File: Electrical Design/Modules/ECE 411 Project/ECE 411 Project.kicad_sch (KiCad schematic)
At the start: 11 parts, among them J1 NJ2FD-V, J2 Conn_01x02_Pin, Q7 PNP, U1 ESP32-C3-WROOM-02, U10 MN3207, U2 LM555xM, U4 PAM8406D, U6 TL072

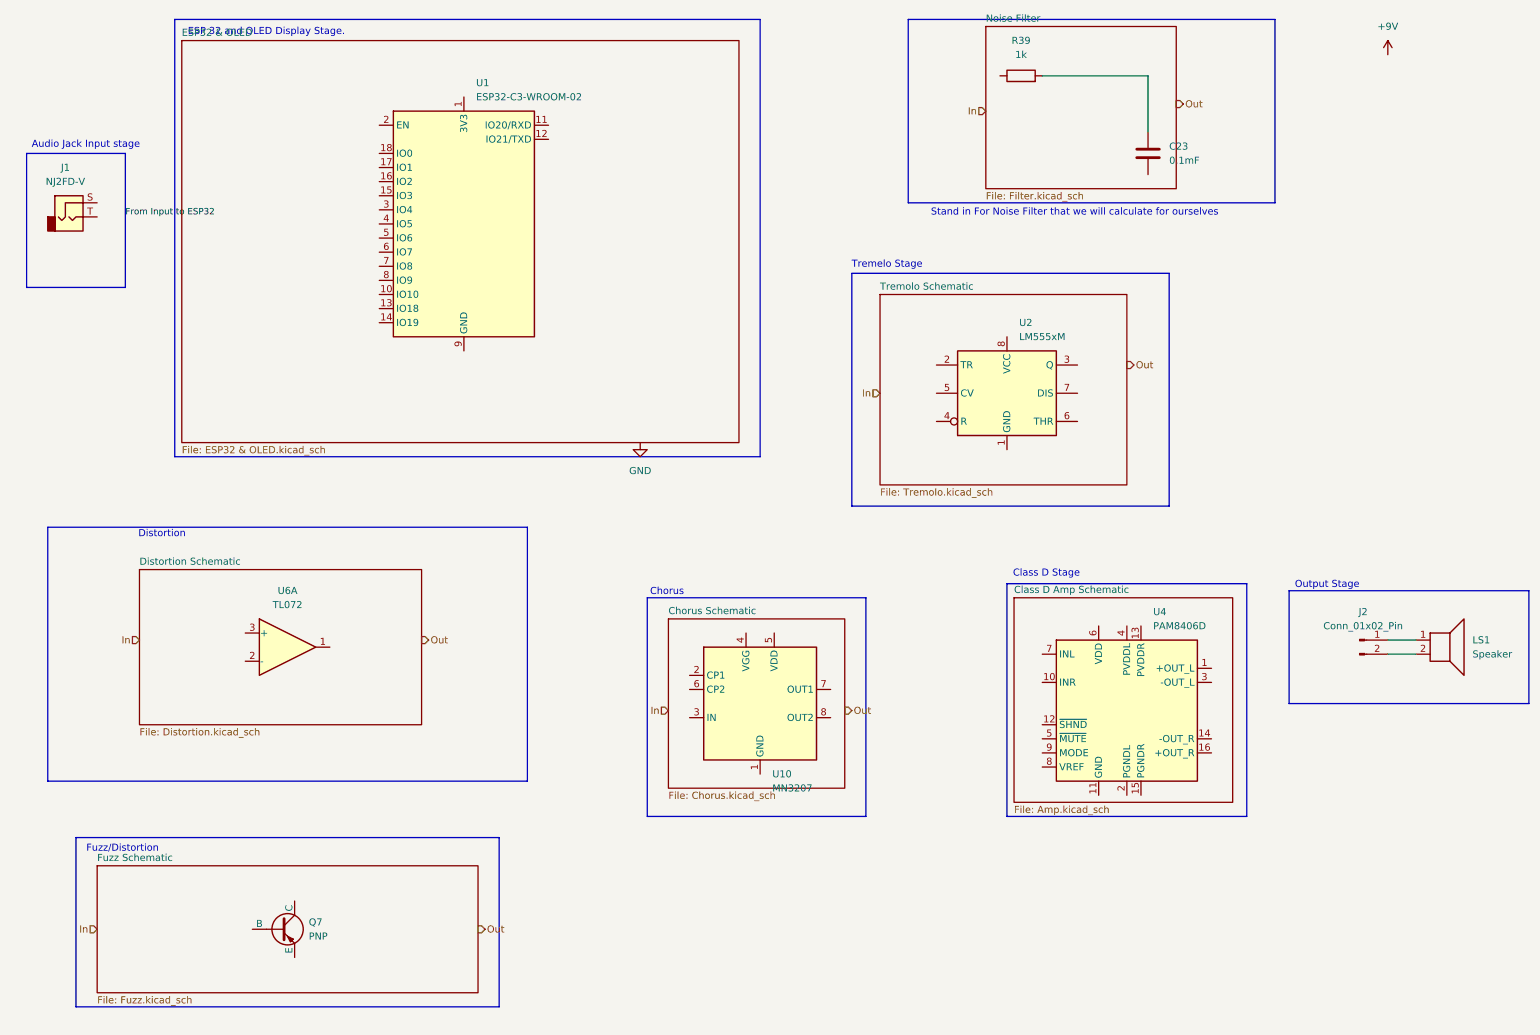
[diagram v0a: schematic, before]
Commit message: Minor changes to schematic wiring
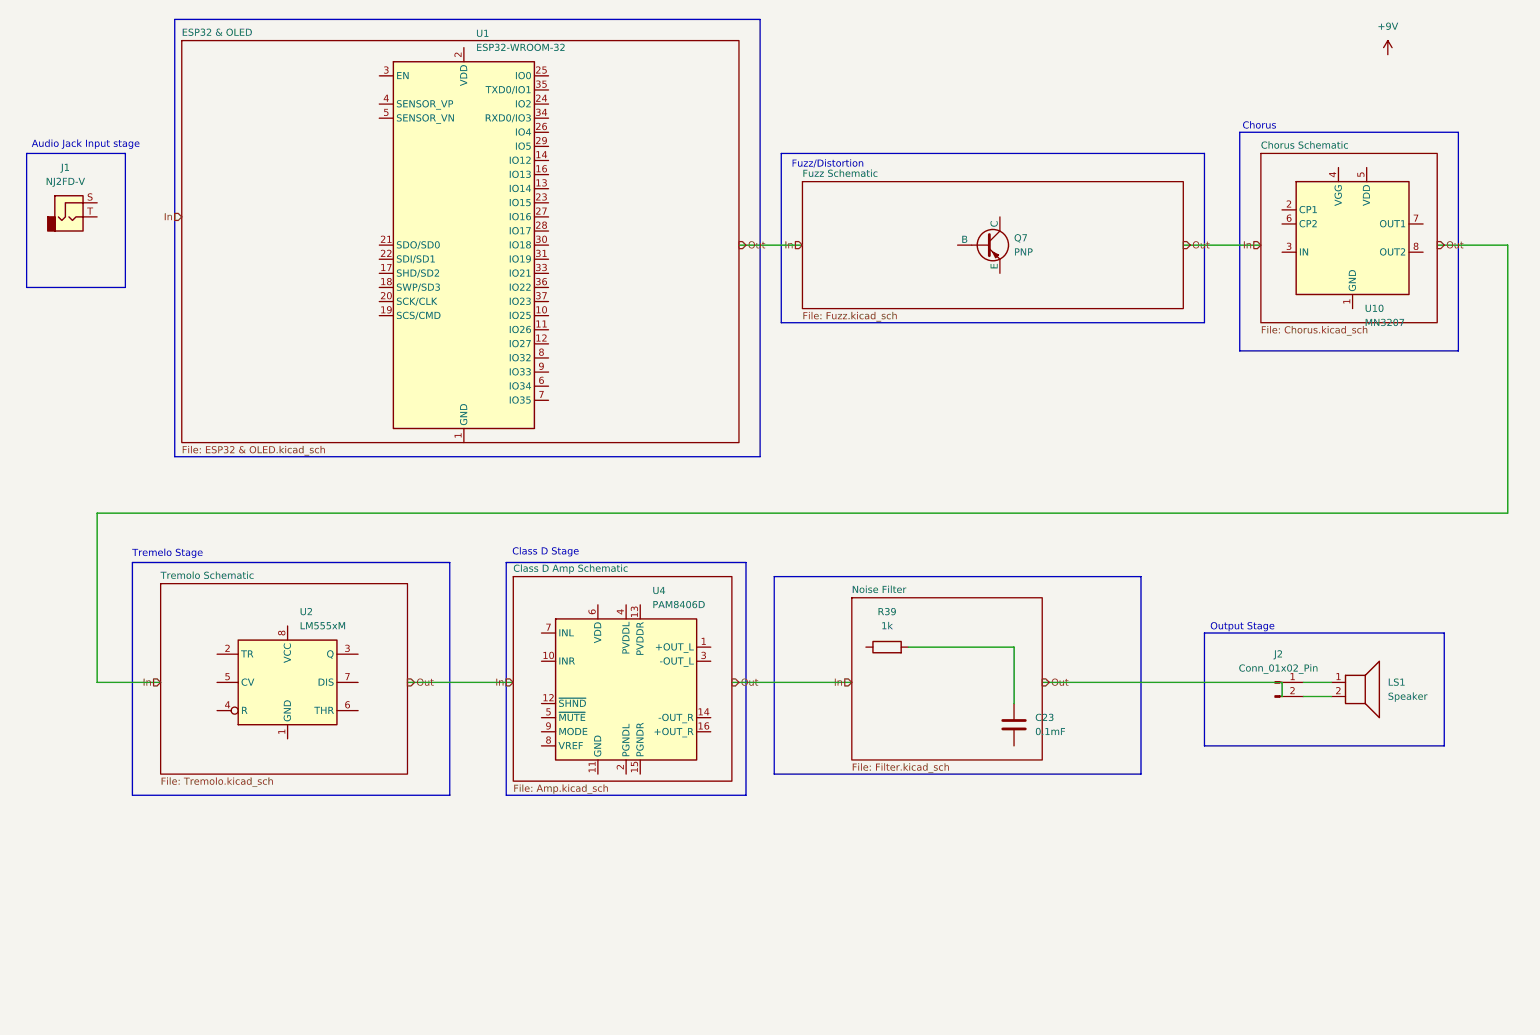
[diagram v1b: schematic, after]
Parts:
- removed U1: ESP32-C3-WROOM-02, RF_Module:ESP32-C3-WROOM-02, symbol RF_Module:ESP32-C3-WROOM-02
- removed U6: TL072, symbol Amplifier_Operational:TL072
- added U1: ESP32-WROOM-32, RF_Module:ESP32-WROOM-32, symbol RF_Module:ESP32-WROOM-32
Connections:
- new net: U1.1 (GND), U1.15 (GND), U1.38 (GND), U1.39 (GND)
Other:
- removed sheet Distortion Schematic
- note removed: "Distortion"
- note removed: "ESP 32 and OLED Display Stage."
- note removed: "Stand in For Noise Filter that we will calculate for ourselves"
- moved on the sheet: C23, J2, LS1, Q7, R39, U10, U2, U4

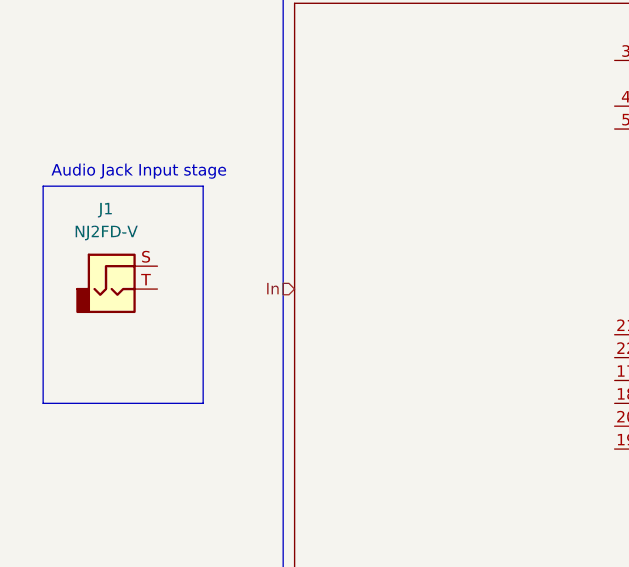
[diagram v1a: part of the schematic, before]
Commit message: Final Touches to Preliminary Schematic
Created Symbol for Small OLED screen and finalized input/output connections for each module
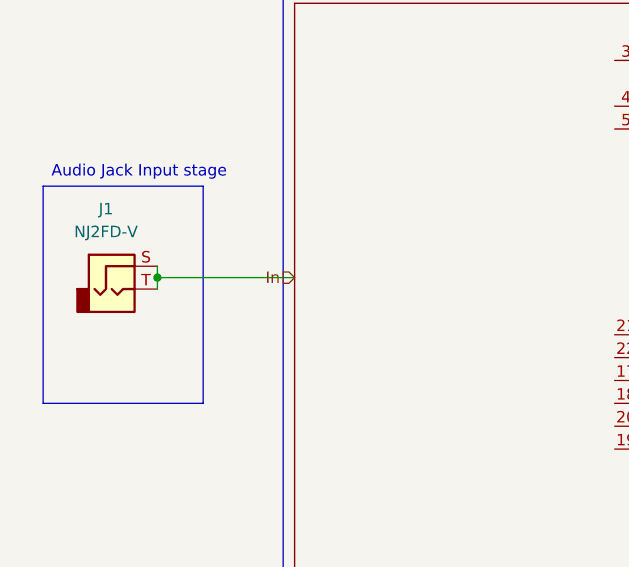
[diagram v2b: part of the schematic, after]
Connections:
- net In: now also J1.S, J1.T
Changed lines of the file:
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@@
 	(generator_version "8.0")
 	(paper "A4")
+	(junction
+		(at 25.4 46.99)
+		(diameter 0)
+		(color 0 0 0 0)
+	)
 	(wire
 		(pts
@@
 	(wire
 		(pts
+			(xy 25.4 45.72) (xy 25.4 46.99)
+		)
+		(stroke
+			(width 0)
+			(type default)
+		)
+	)
+	(wire
+		(pts
 			(xy 25.4 101.6) (xy 25.4 132.08)
 		)
@@
 	(wire
 		(pts
+			(xy 25.4 46.99) (xy 25.4 48.26)
+		)
+		(stroke
+			(width 0)
+			(type default)
+		)
+	)
+	(wire
+		(pts
 			(xy 279.4 101.6) (xy 25.4 101.6)
 		)
@@
 		(pts
 			(xy 25.4 132.08) (xy 36.83 132.08)
+		)
+		(stroke
+			(width 0)
+			(type default)
+		)
+	)
+	(wire
+		(pts
+			(xy 25.4 46.99) (xy 40.64 46.99)
 		)
 		(stroke
@@
 	(hierarchical_label "In"
 		(shape input)
-		(at 40.64 48.26 180)
-		(fields_autoplaced yes)
-		(effects
+		(at 40.64 46.99 180)
+		(fields_autoplaced yes)
+		(effects

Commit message: kicad business
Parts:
- removed J1: NJ2FD-V, Connector_Audio:Jack_6.35mm_Neutrik_NJ2FD-V_Vertical, symbol Connector_Audio:NJ2FD-V
- removed J2: Conn_01x02_Pin, symbol Connector:Conn_01x02_Pin
- removed LS1: Speaker, symbol Device:Speaker
- removed Q7: PNP, symbol Simulation_SPICE:PNP
- removed U1: ESP32-WROOM-32, RF_Module:ESP32-WROOM-32, symbol RF_Module:ESP32-WROOM-32
- removed U10: MN3207, symbol Audio:MN3207
- removed U2: LM555xM, Package_SO:SOIC-8_3.9x4.9mm_P1.27mm, symbol Timer:LM555xM
- removed U4: PAM8406D, Package_SO:SOP-16_3.9x9.9mm_P1.27mm, symbol Amplifier_Audio:PAM8406D
- added O1: Neutrik speakON 2-pin Connector, symbol Connector_Audio:SpeakON_NL2
- added OLED1: ~, symbol Project Specific Library:OLED_SSD1306
- added R38, R54, R55, R56, R57, R58, R59, R60, R61, R62, R63, R64: 1k, symbol Device:R
- added SW12, SW13, SW14, SW15, SW16, SW17, SW18, SW19, SW20, SW21, SW22: SW_Push, symbol Switch:SW_Push
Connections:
- net GND: now reaches R39.1
- net GND: now also OLED1.1 (GND), R64.2
- net at R39.2: now also C23.2; no longer C23.1
- new net: R60.2, R61.1, SW19.1
- new net: R57.2, R58.1, SW16.1
- new net: R58.2, R59.1, SW17.1
- new net: R38.2, R54.1, SW12.1
- new net: R61.2, R62.1, SW20.1
- new net: R59.2, R60.1, SW18.1
- new net: R63.2, R64.1, SW22.1
- new net: R54.2, R55.1, SW13.1
- new net: R55.2, R56.1, SW14.1
- new net: R56.2, R57.1, SW15.1
- new net: R62.2, R63.1, SW21.1
- new net +3V3: OLED1.2 (VCC), R38.1
- new net AMPIN: C23.1
- new net IO0: SW12.2, SW13.2, SW14.2, SW15.2, SW16.2, SW17.2, SW18.2, SW19.2, SW20.2, SW21.2, SW22.2
- new net SCL: OLED1.4 (SCL)
- new net SDA: OLED1.3 (SDA)
- new net SPK+: O1.1+
- new net SPK-: O1.1-
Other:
- sheet Chorus Schematic renamed Chorus Effect
- sheet Class D Amp Schematic renamed Class-D Amplification
- sheet Tremolo Schematic renamed Tremolo Effect
- removed sheet Noise Filter
- note added: "Fuzz/Distortion Effect"
- note added: "Notes: - Power supply design TBD. All effects are ±9V supplies. MCU will operate off of either 3V3 or 5V. - Power supply connector TBD (likely 5mm barrel jack) - MCU will control which effects active, how this will be done is TBD (likely relays)"
- note added: "Output Filtering"
- note added: "Output to 8Ω Speaker"
- note removed: "Audio Jack Input stage"
- note removed: "Chorus"
- note removed: "Class D Stage"
- note removed: "Fuzz/Distortion"
- note removed: "Output Stage"
- note removed: "Tremelo Stage"
- company: (none) -> Portland State University
- title: (none) -> PedalSynth PWM Synthesizer
- moved on the sheet: C23, R39

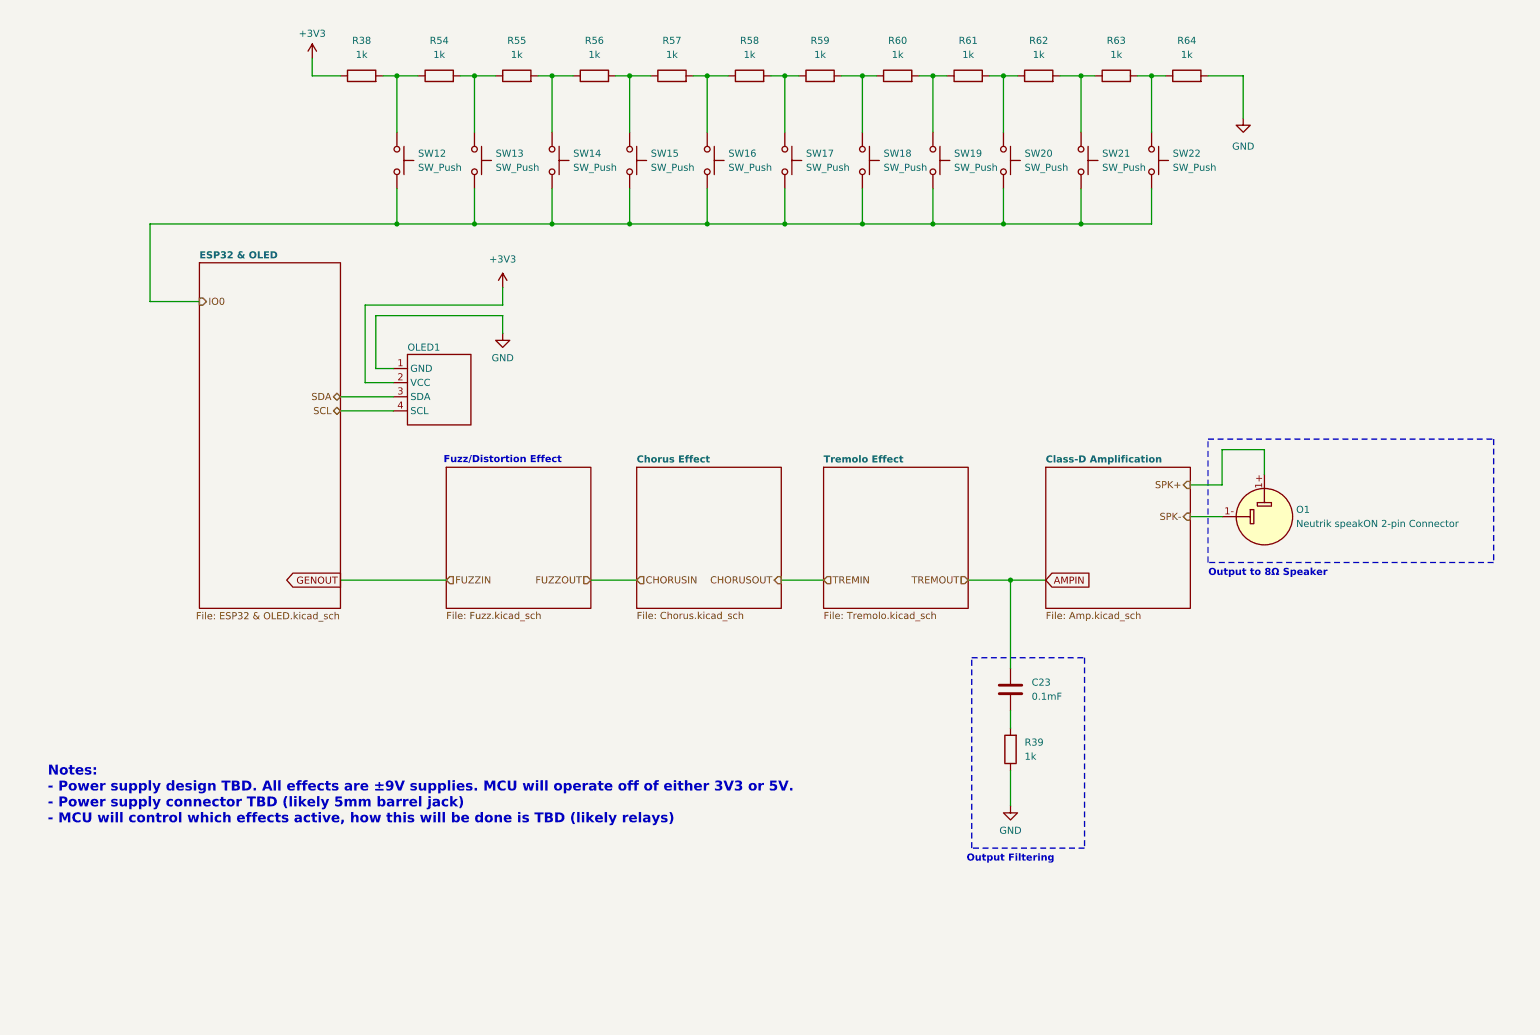
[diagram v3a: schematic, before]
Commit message: add psu and fix schematic
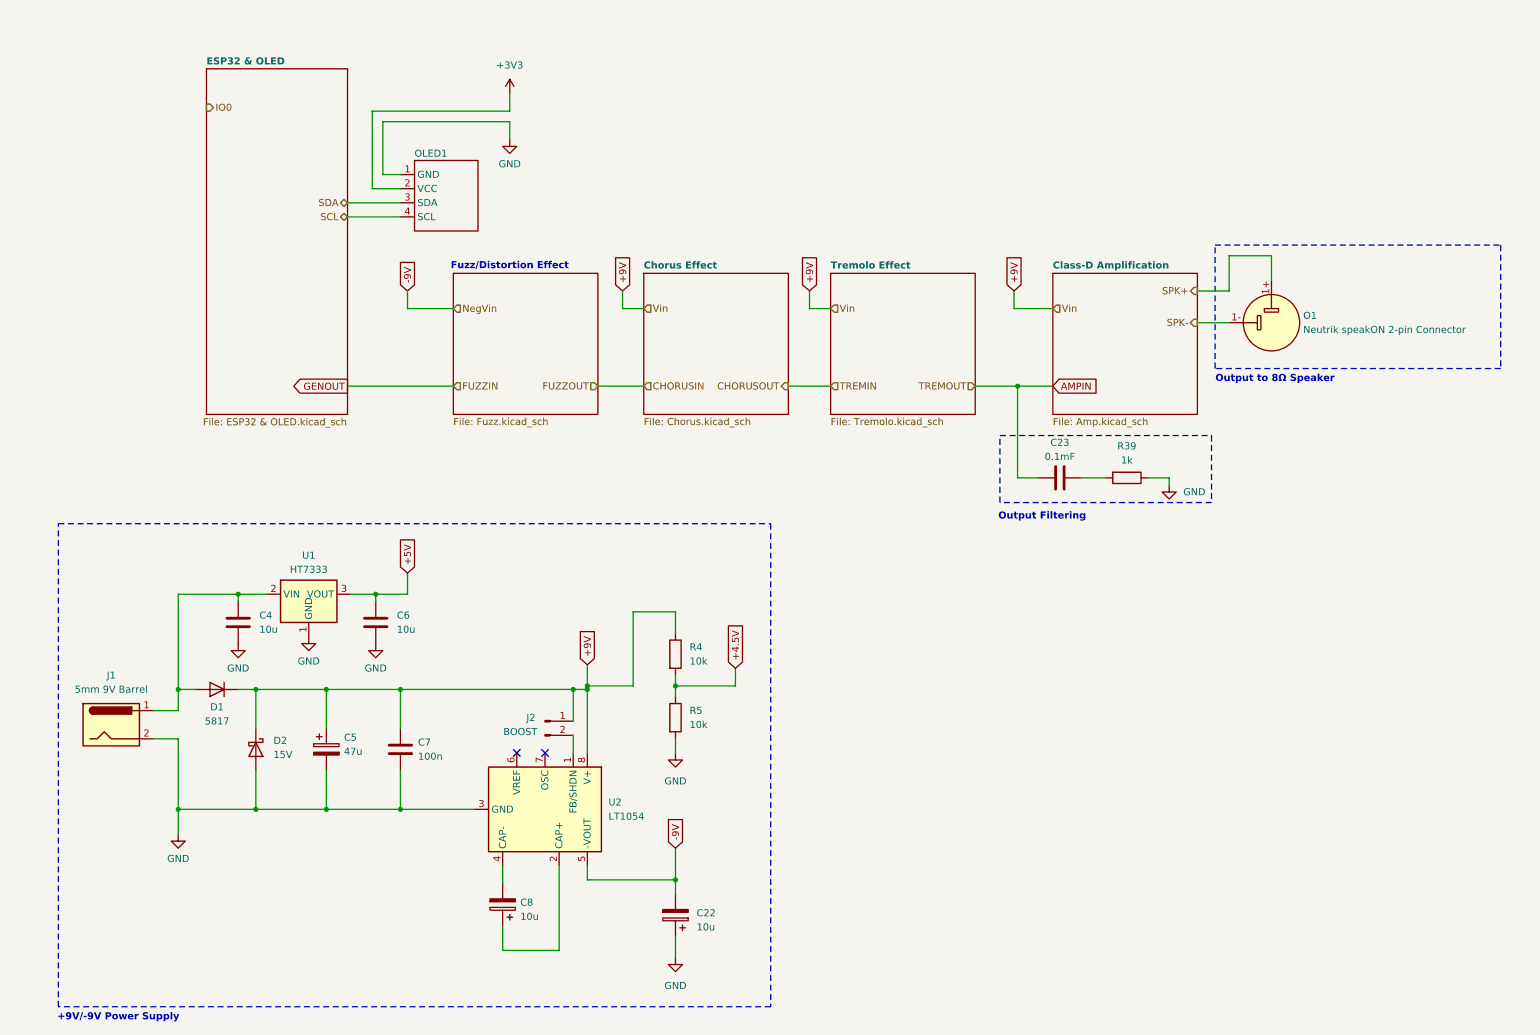
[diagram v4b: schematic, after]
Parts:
- removed R38, R54, R55, R56, R57, R58, R59, R60, R61, R62, R63, R64: 1k, symbol Device:R
- removed SW12, SW13, SW14, SW15, SW16, SW17, SW18, SW19, SW20, SW21, SW22: SW_Push, symbol Switch:SW_Push
- added C22, C8: 10u, symbol Device:C_Polarized
- added C4, C6: 10u, symbol Device:C
- added C5: 47u, symbol Device:C_Polarized
- added C7: 100n, symbol Device:C
- added D1: 5817, symbol Device:D
- added D2: 15V, symbol Device:D_Schottky
- added J1: 5mm 9V Barrel, symbol Connector:Barrel_Jack
- added J2: BOOST, symbol Connector:Conn_01x02_Pin
- added R4, R5: 10k, symbol Device:R
- added U1: HT7333, Package_TO_SOT_SMD:SOT-89-3, symbol Regulator_Linear:HT75xx-1-SOT89
- added U2: LT1054, symbol Regulator_SwitchedCapacitor:LT1054
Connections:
- net GND: now also C22.1, C4.2, C5.2, C6.2, C7.2, D2.2 (A), J1.2, R5.2, U1.1 (GND), U2.3 (GND)
- new net: C4.1, D1.2 (A), J1.1, U1.2 (VIN)
- new net: J2.2 (Pin_2), U2.1 (FB/SHDN)
- new net: C8.1, U2.2 (CAP+)
- new net: C8.2, U2.4 (CAP-)
- new net +4.5V: R4.2, R5.1
- new net +5V: C6.1, U1.3 (VOUT)
- new net +9V: C5.1, C7.1, D1.1 (K), D2.1 (K), J2.1 (Pin_1), R4.1, U2.8 (V+)
- new net -9V: C22.2, U2.5 (-VOUT)
- no-connect marks 0 -> 2
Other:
- note added: "+9V/-9V Power Supply"
- note removed: "Notes: - Power supply design TBD. All effects are ±9V supplies. MCU will operate off of either 3V3 or 5V. - Power supply connector TBD (likely 5mm barrel jack) - MCU will control which effects active, how this will be done is TBD (likely relays)"
- moved on the sheet: C23, O1, OLED1, R39
